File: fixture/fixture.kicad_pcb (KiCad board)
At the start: 2 copper layers, 100 x 100 mm, 39 parts, among them J1 Conn_Coaxial, J10 Conn_Coaxial, J11 Conn_Coaxial, J12 Conn_Coaxial, J13 Conn_Coaxial, J14 Conn_Coaxial, J15 Conn_Coaxial, J16 Conn_Coaxial, J17 Conn_Coaxial, J18 Conn_01x01, J19 Conn_01x01, J2 Conn_Coaxial, J20 Conn_01x01, J21 Conn_01x01, J22 Conn_Coaxial, J23 Conn_Coaxial, J24 Conn_Coaxial, J25 Conn_Coaxial, J27 Conn_Coaxial, J28 Conn_01x02, J29 Conn_Coaxial, J3 Conn_Coaxial, J30 Conn_01x01, J31 Conn_01x01, J32 Conn_Coaxial, J4 Conn_02x08_Counter_Clockwise, J5 Conn_02x08_Counter_Clockwise, J6 Conn_Coaxial, J7 Conn_Coaxial, J8 Conn_Coaxial, J9 Conn_Coaxial

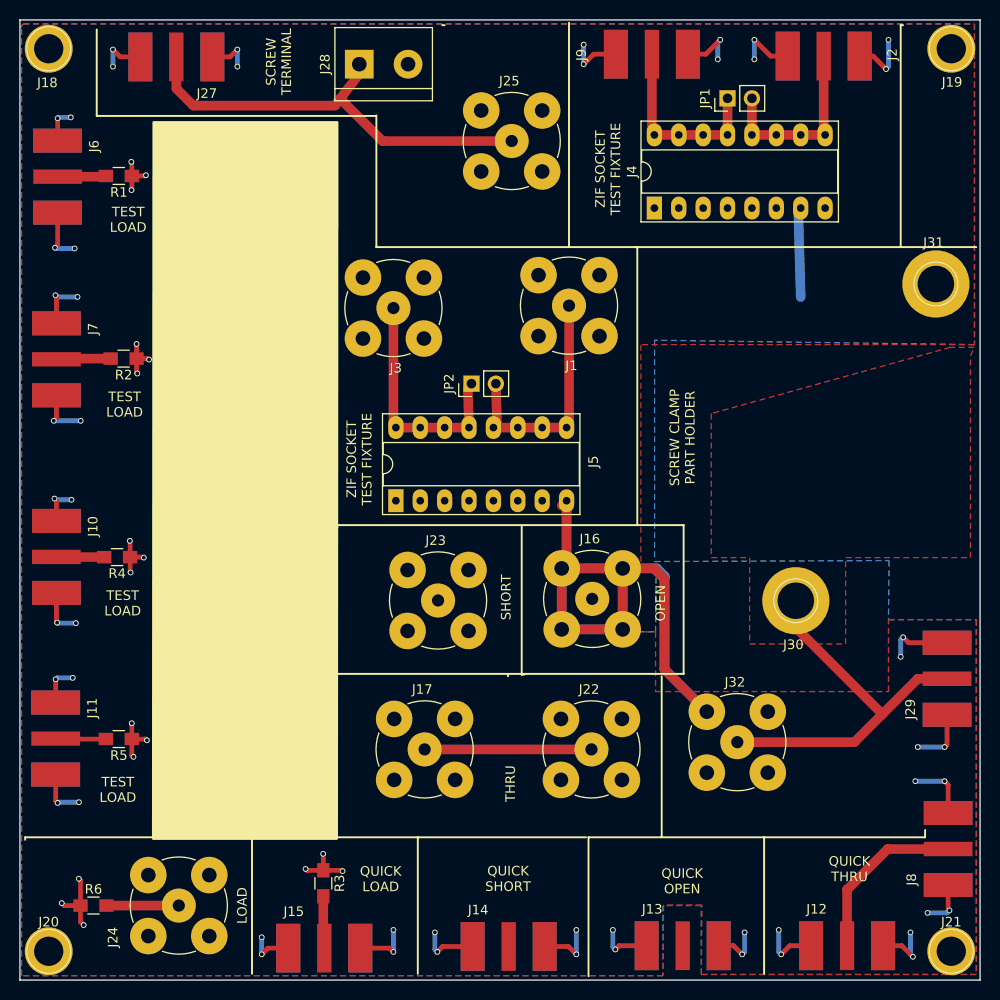
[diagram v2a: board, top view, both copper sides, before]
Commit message: Added vacuum holes to fixture
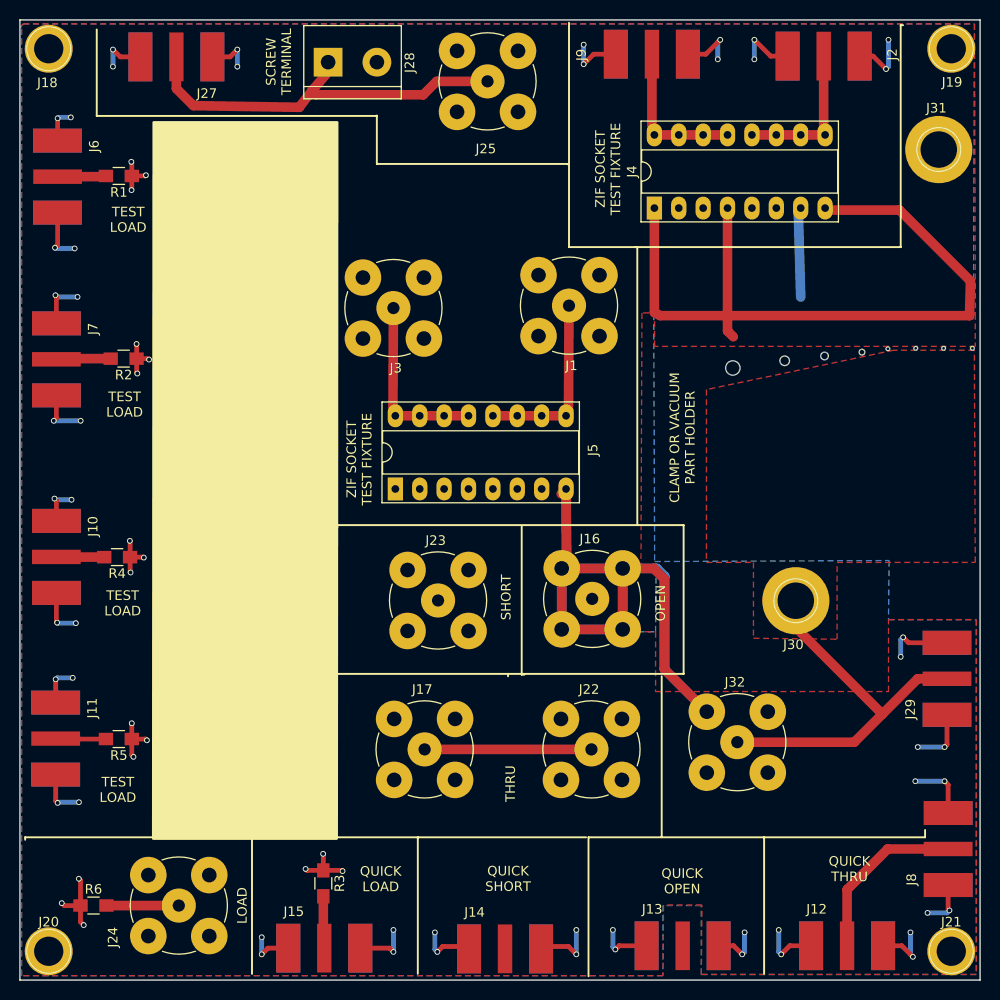
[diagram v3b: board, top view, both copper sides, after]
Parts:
- removed JP1, JP2: Jumper_NO_Small, Pin_Headers:Pin_Header_Straight_1x02_Pitch2.54mm
- added ?: , fixture:AirHole, F.Cu at (146.2, 84.2)
- added ?: , fixture:AirHole, F.Cu at (140.4, 84.2)
- added ?: , fixture:AirHole, F.Cu at (149.2, 84.2)
- added ?: , fixture:AirHole, F.Cu at (133.8, 85.0)
- added ?: , fixture:AirHole, F.Cu at (137.7, 84.6)
- added ?: , fixture:AirHole, F.Cu at (124.2, 86.2)
- added ?: , fixture:AirHole, F.Cu at (143.3, 84.2)
- added ?: , fixture:AirHole, F.Cu at (129.7, 85.5)
- moved J31 14.0 mm to (145.7, 63.5)
- moved J25 6.70 mm to (98.7, 56.4)
- moved J28 3.25 mm to (82.1, 54.4)
- moved J5 1.23 mm to (89.1, 98.8)
- moved J14 0.45 mm to (100.5, 146.8)
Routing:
- net GND: track 293.4 -> 375.2 mm
- net Net-(J1-Pad1): track 25.7 -> 19.7 mm
- net Net-(J3-Pad1): track 26.6 -> 20.6 mm
- net Net-(J4-Pad13): track 19.9 -> 16.1 mm
- net Net-(J2-Pad1): track 19.7 -> 15.9 mm
- net Net-(J25-Pad1): track 45.4 -> 41.7 mm
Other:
- board text added: "CLAMP OR VACUUM PART HOLDER"
- board text removed: "SCREW CLAMP PART HOLDER"

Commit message: Modified fixture for larger holes for ZIF socket
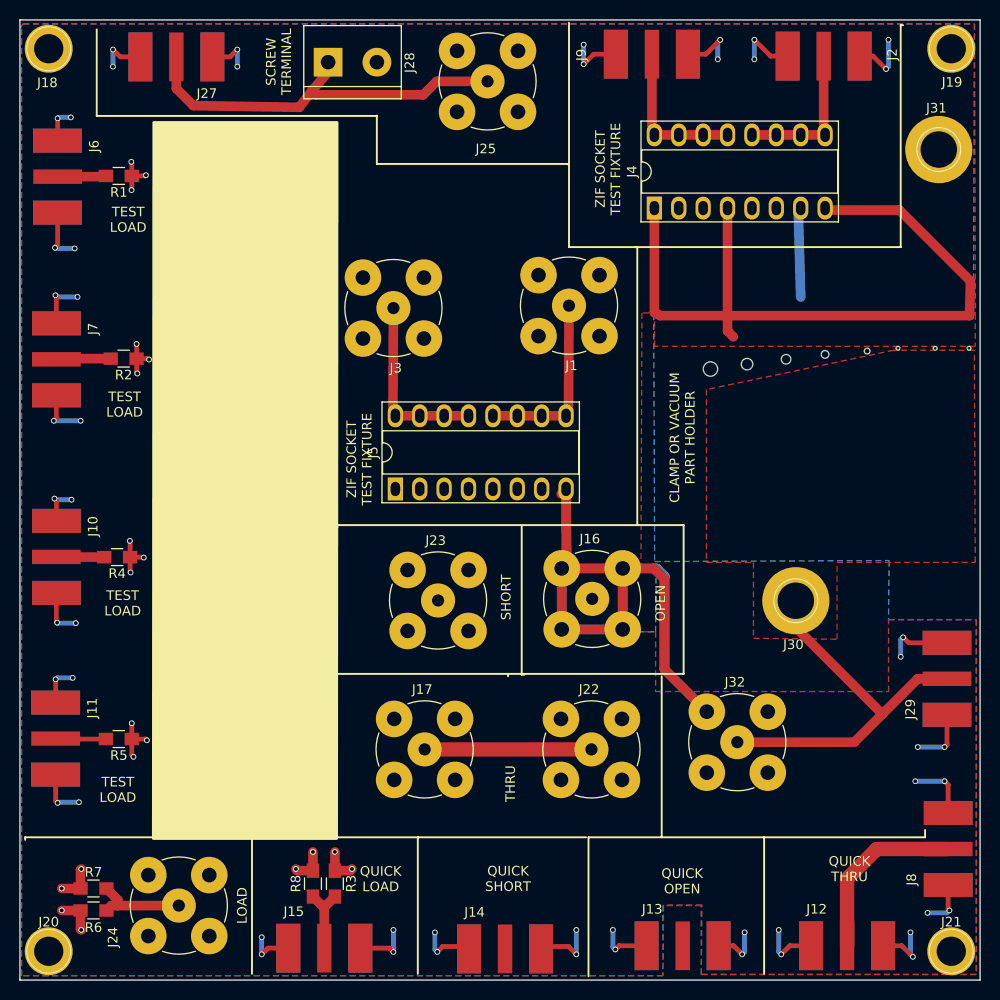
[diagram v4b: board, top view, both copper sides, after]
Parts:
- removed the ? at (146.2, 84.2)
- removed the ? at (140.4, 84.2)
- removed the ? at (149.2, 84.2)
- removed the ? at (133.8, 85.0)
- removed the ? at (137.7, 84.6)
- removed the ? at (124.2, 86.2)
- removed the ? at (143.3, 84.2)
- removed the ? at (129.7, 85.5)
- added ?: , fixture:AirHole, F.Cu at (148.8, 84.2)
- added ?: , fixture:AirHole, F.Cu at (145.3, 84.2)
- added ?: , fixture:AirHole, F.Cu at (138.2, 84.5)
- added ?: , fixture:AirHole, F.Cu at (141.4, 84.2)
- added ?: , fixture:AirHole, F.Cu at (125.7, 85.9)
- added ?: , fixture:AirHole, F.Cu at (121.9, 86.4)
- added ?: , fixture:AirHole, F.Cu at (133.9, 84.8)
- added ?: , fixture:AirHole, F.Cu at (129.8, 85.3)
- added R7: R, Resistors_SMD:R_0805_HandSoldering, F.Cu at (57.7, 140.5)
- added R8: R, Resistors_SMD:R_0805_HandSoldering, F.Cu at (80.5, 140.0)
- J4, J5: footprint Housings_DIP:DIP-16_W7.62mm_Socket_LongPads -> fixture:ZIFSocket16pin
- moved R3 1.20 mm to (82.8, 140.0)
- moved R6 0.51 mm to (57.7, 142.7)
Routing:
- net GND: track 375.2 -> 378.1 mm, vias 70 -> 72
- net Net-(J24-Pad1): track 7.54 -> 10.0 mm
- net Net-(J15-Pad1): track 5.44 -> 7.65 mm
- net Net-(J12-Pad1): track 18.1 -> 18.8 mm

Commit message: Changed fixture loads to have less capacitance
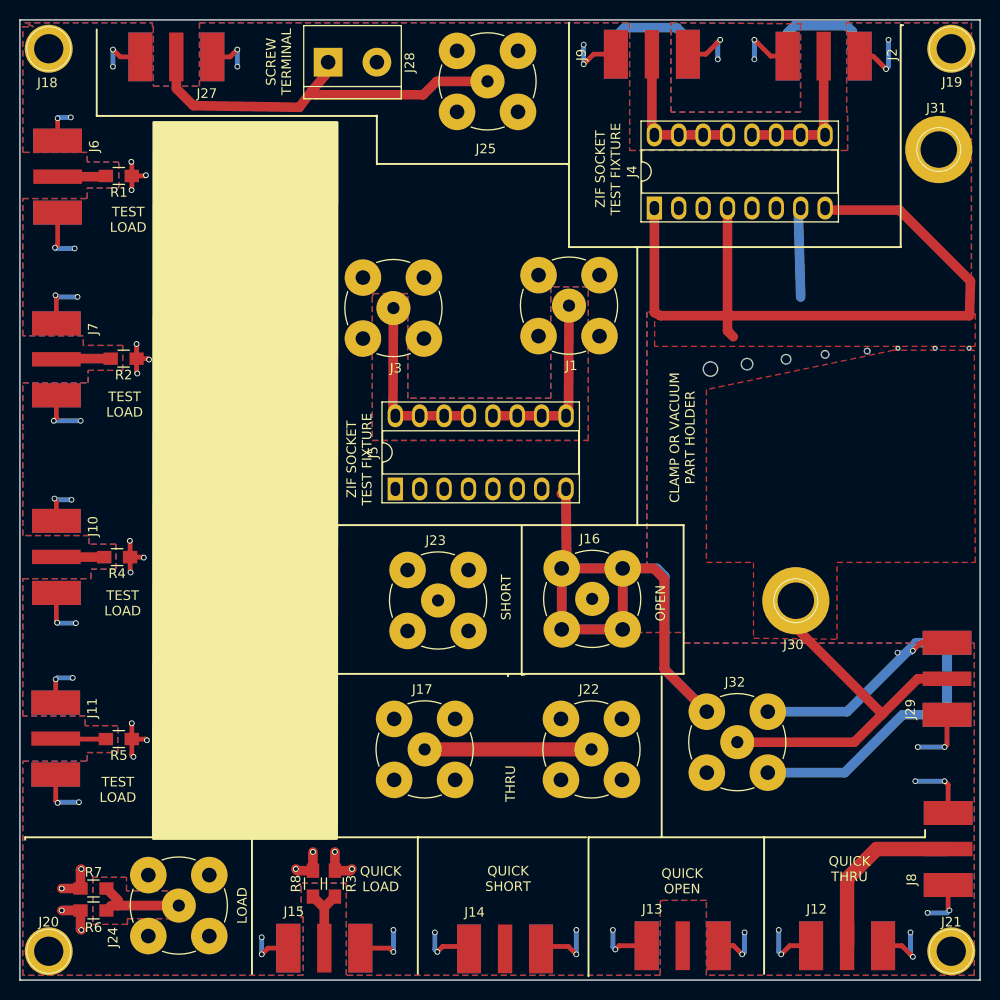
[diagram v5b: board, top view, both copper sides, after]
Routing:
- net GND: track 378.1 -> 451.4 mm

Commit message: Move components around on board, adjusted fixture, added touchscreen disables
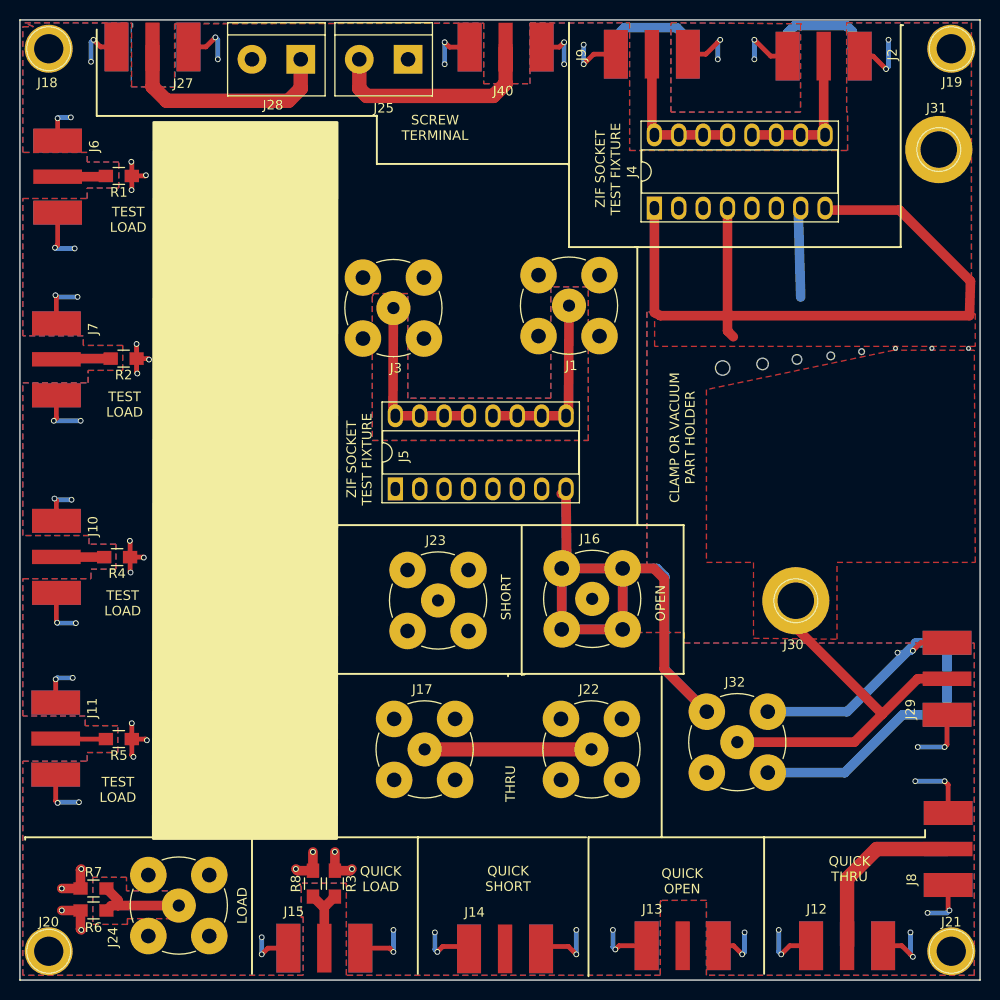
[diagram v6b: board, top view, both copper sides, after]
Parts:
- removed ? (x8): , fixture:AirHole
- added J26: Conn_01x01, fixture:AirHole, F.Cu at (123.2, 86.2)
- added J33: Conn_01x01, fixture:AirHole, F.Cu at (134.4, 85.0)
- added J34: Conn_01x01, fixture:AirHole, F.Cu at (145.0, 84.2)
- added J35: Conn_01x01, fixture:AirHole, F.Cu at (130.9, 85.4)
- added J36: Conn_01x01, fixture:AirHole, F.Cu at (127.3, 85.8)
- added J37: Conn_01x01, fixture:AirHole, F.Cu at (148.8, 84.2)
- added J38: Conn_01x01, fixture:AirHole, F.Cu at (137.7, 84.5)
- added J39: Conn_01x01, fixture:AirHole, F.Cu at (141.2, 84.2)
- added J40: Conn_Coaxial, fixture:Amphenol_RF_SMA_132289, F.Cu at (100.6, 52.8)
- J25: value Conn_Coaxial -> Conn_01x02; footprint Connectors:bnc-ci -> Connectors_Terminal_Blocks:TerminalBlock_bornier-2_P5.08mm
- moved J25 8.59 mm to (90.4, 54.1), turned to 180 degrees
- moved J28 2.87 mm to (79.2, 54.1), turned to 180 degrees
- moved J27 2.69 mm to (63.8, 52.8)
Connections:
- J25 pad 1: Net-(J25-Pad1) -> GND
- J25 pad 2: GND -> Net-(J25-Pad2)
- J27 pad 1: Net-(J25-Pad1) -> Net-(J27-Pad1)
- J28 pad 1: Net-(J25-Pad1) -> Net-(J27-Pad1)
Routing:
- net Net-(J25-Pad1): track 41.7 -> 0.00 mm
- net Net-(J27-Pad1): track 0.00 -> 23.8 mm
- net Net-(J25-Pad2): track 0.00 -> 22.9 mm
- net GND: track 451.4 -> 462.4 mm, vias 72 -> 76
